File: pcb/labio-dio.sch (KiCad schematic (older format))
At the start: 0 parts

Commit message: add schematics for display and dio (dpad, servo, motor, encoder)
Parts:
- added C? (x5): C_Small, symbol C_Small
- added C? (x2): 0.1uF, symbol C_Small
- added P? (x5): CONN_01X03, symbol CONN_01X03
- added P? (x2): CONN_01X05, symbol CONN_01X05
- added P? (x3): CONN_01X02, symbol CONN_01X02
- added SW? (x5): SW_PUSH, symbol SW_PUSH
- added U?: L298P, symbol L298P
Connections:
- new net: P?.2 (P2), P?.4 (P4), P?.4 (P4)
- new net DPAD_CENTER: C?.1, SW?.1
- new net DPAD_DOWN: C?.1, SW?.1
- new net DPAD_LEFT: C?.1, SW?.1
- new net DPAD_RIGHT: C?.1, SW?.1
- new net DPAD_UP: C?.1, SW?.1
- new net ENC0_A: P?.3 (P3)
- new net ENC0_B: P?.5 (P5)
- new net ENC0_IDX: P?.2 (P2)
- new net ENC1_A: P?.3 (P3)
- new net ENC1_B: P?.5 (P5)
- new net ENC1_IDX: P?.2 (P2)
- new net GND: C?.2, C?.2, C?.2, C?.2, C?.2, C?.2, C?.2, P?.1 (P1), P?.1 (P1), P?.1 (P1), P?.1 (P1), P?.1 (P1), P?.2 (P2), SW?.2, SW?.2, SW?.2, U?.1 (GND), U?.10 (GND), U?.11 (GND), U?.20 (GND)
- new net MOTOR_IN1: U?.7 (IN1)
- new net MOTOR_IN2: U?.9 (IN2)
- new net MOTOR_IN3: U?.13 (IN3)
- new net MOTOR_IN4: U?.15 (IN4)
- new net MOTOR_OUT1: P?.1 (P1), U?.4 (OUT1)
- new net MOTOR_OUT2: P?.2 (P2), U?.5 (OUT2)
- new net MOTOR_OUT3: P?.1 (P1), U?.16 (OUT3)
- new net MOTOR_OUT4: P?.2 (P2), U?.17 (OUT4)
- new net MOTOR_SENSEA: P?.3 (P3), U?.2 (SENSEA)
- new net MOTOR_SENSEB: P?.2 (P2), U?.19 (SENSEB)
- new net PWM0: P?.3 (P3), U?.8 (ENABLEA)
- new net PWM1: P?.3 (P3), U?.14 (ENABLEB)
- new net VDD_3V3: C?.1, P?.1 (P1), U?.12 (VSS)
- new net VDD_5V: P?.3 (P3), P?.3 (P3)
- new net VMOTOR: C?.1, P?.1 (P1), P?.1 (P1), U?.6 (VS)
- new net VSERVO: P?.2 (P2), P?.2 (P2), P?.2 (P2)
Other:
- note added: "D-Pad\nUse RPi pull-ups with optional C for decoupling.\nIndividual IO lines for interrupts."
- note added: "Motor Driver"
- note added: "Quadrature Encoder\nUS Digital S1 Pinout.\nJumper for 3V3 or 5V power."
- note added: "Servos\nGround, voltage, signal headers.\nJumper for VMOTOR or 5V power."

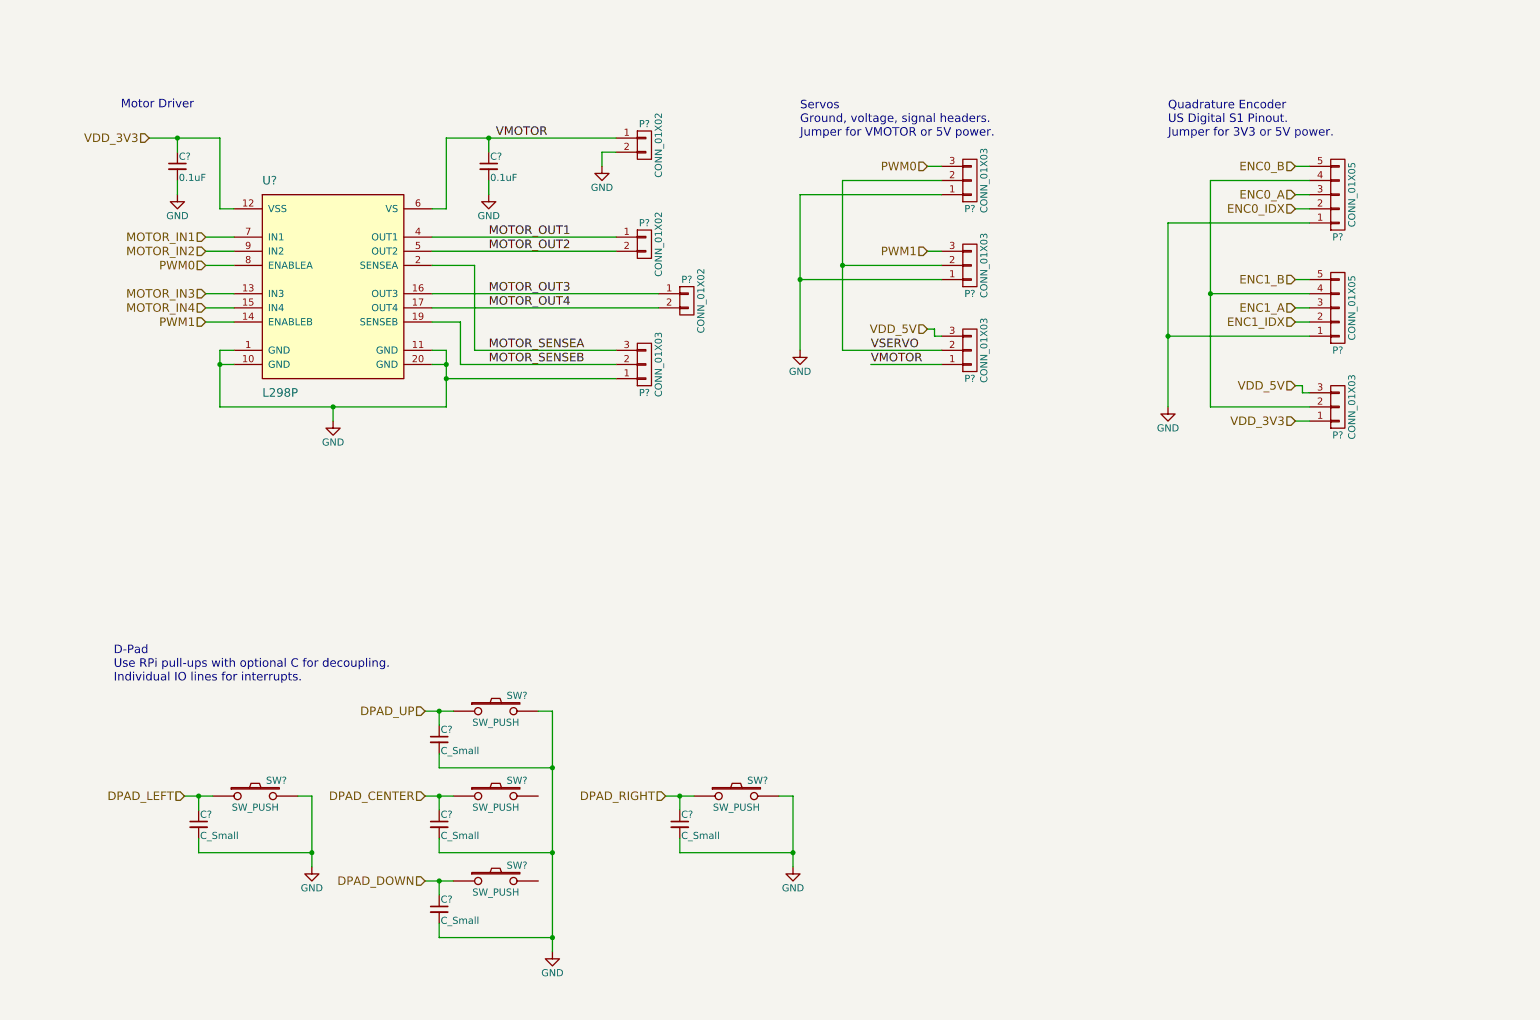
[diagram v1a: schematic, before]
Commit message: add imu sensors, make top level connections
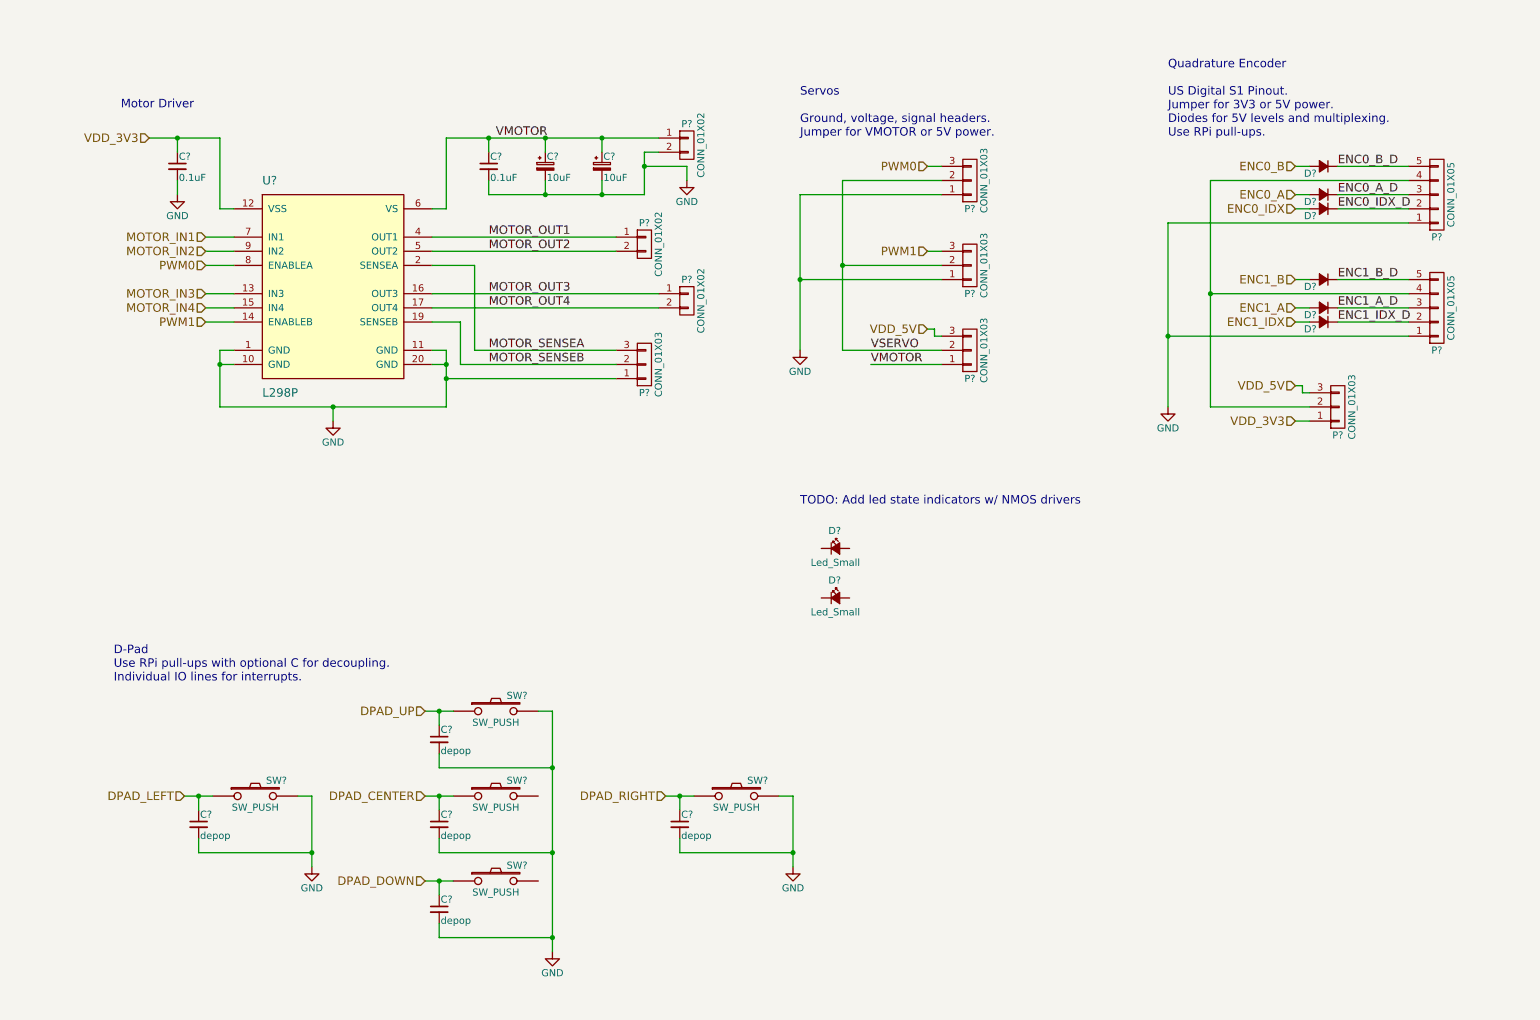
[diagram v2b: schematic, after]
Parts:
- added C? (x2): 10uF, symbol CP_Small
- added D? (x2): Led_Small, symbol Led_Small
- added D? (x6): D_Small, symbol D_Small
- C? (x5): value C_Small -> depop
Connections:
- net ENC0_A: now also D?.2 (A); no longer P?.3 (P3)
- net ENC0_B: now also D?.2 (A); no longer P?.5 (P5)
- net ENC0_IDX: now also D?.2 (A); no longer P?.2 (P2)
- net ENC1_A: now also D?.2 (A); no longer P?.3 (P3)
- net ENC1_B: now also D?.2 (A); no longer P?.5 (P5)
- net ENC1_IDX: now also D?.2 (A); no longer P?.2 (P2)
- net GND: now also C?.2, C?.2
- net VMOTOR: now also C?.1, C?.1
- new net ENC0_A_D: D?.1 (K), P?.3 (P3)
- new net ENC0_B_D: D?.1 (K), P?.5 (P5)
- new net ENC0_IDX_D: D?.1 (K), P?.2 (P2)
- new net ENC1_A_D: D?.1 (K), P?.3 (P3)
- new net ENC1_B_D: D?.1 (K), P?.5 (P5)
- new net ENC1_IDX_D: D?.1 (K), P?.2 (P2)
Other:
- note added: "Quadrature Encoder\n\nUS Digital S1 Pinout.\nJumper for 3V3 or 5V power.\nDiodes for 5V levels and multiplexing.\nUse RPi pull-ups."
- note added: "Servos\n\nGround, voltage, signal headers.\nJumper for VMOTOR or 5V power."
- note added: "TODO: Add led state indicators w/ NMOS drivers"
- note removed: "Quadrature Encoder\nUS Digital S1 Pinout.\nJumper for 3V3 or 5V power."
- note removed: "Servos\nGround, voltage, signal headers.\nJumper for VMOTOR or 5V power."
- moved on the sheet: P?

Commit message: finish rpi to module connections
* use dip switches to disable/configure blocks
* add light sensor
* fix motor controller sense resistors
* fix overused jtag probe pins
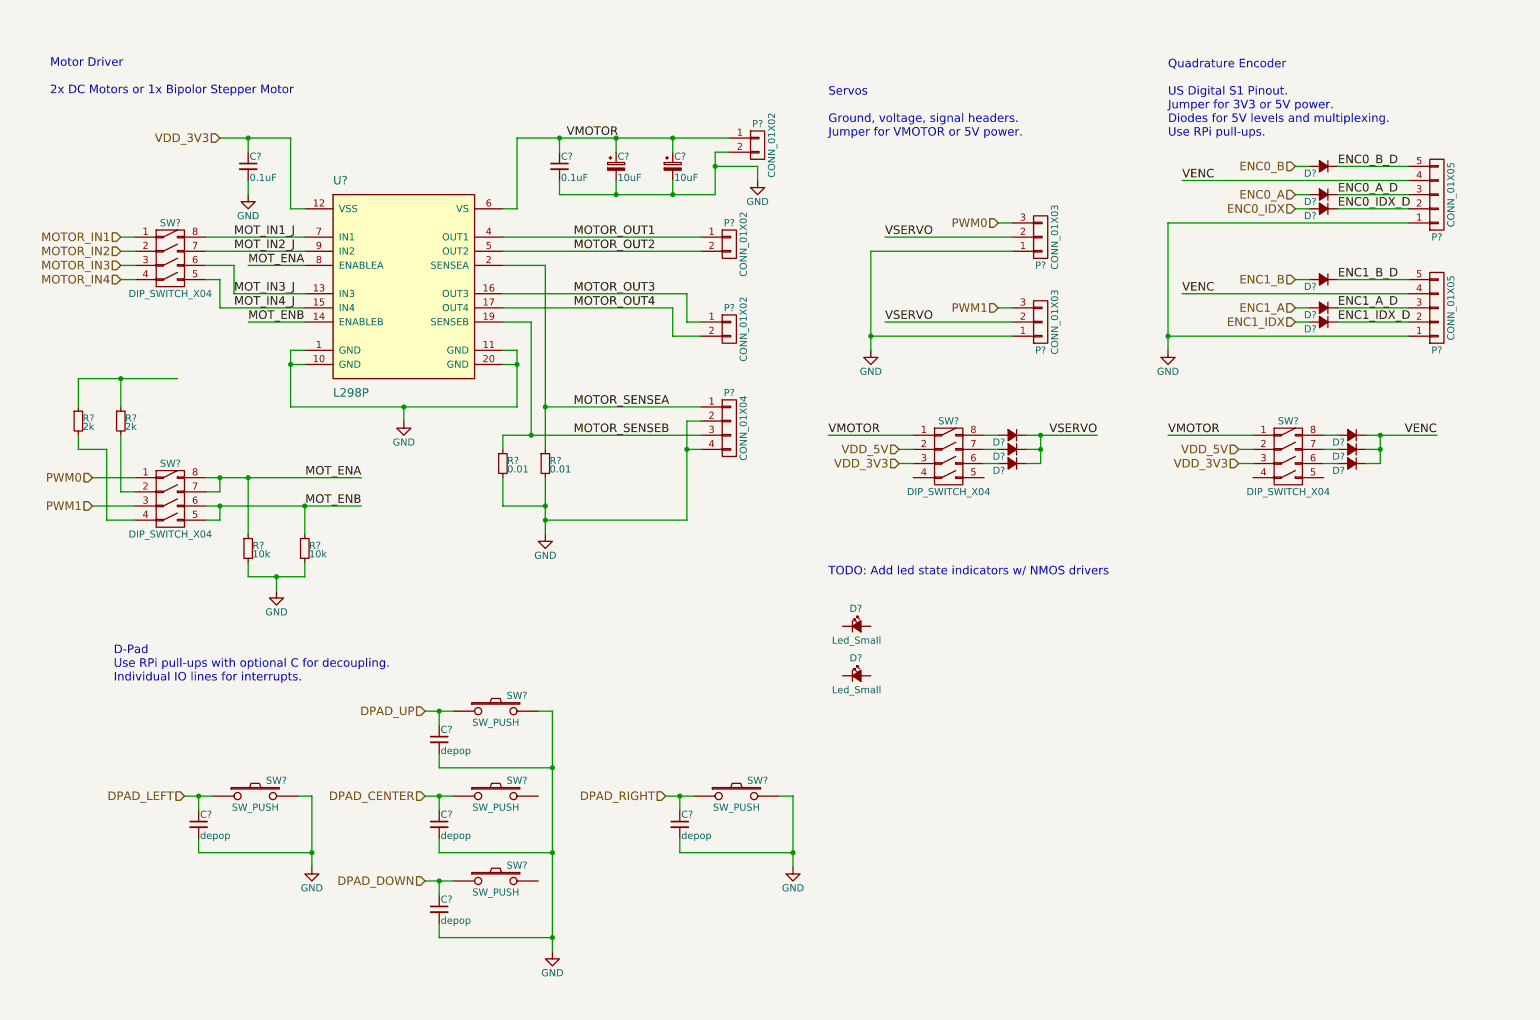
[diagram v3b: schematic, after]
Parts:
- removed P? (x3): CONN_01X03, symbol CONN_01X03
- added D? (x6): D_Small, symbol D_Small
- added P?: CONN_01X04, symbol CONN_01X04
- added R? (x2): 0.01, symbol R_Small
- added R? (x2): 10k, symbol R_Small
- added R? (x2): 2k, symbol R_Small
- added SW? (x4): DIP_SWITCH_X04, symbol DIP_SWITCH_X04
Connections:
- net GND: now also P?.2 (P2), P?.4 (P4), R?.2, R?.2, R?.2, R?.2
- net MOTOR_IN1: now also SW?.1 (1A); no longer U?.7 (IN1)
- net MOTOR_IN2: now also SW?.2 (2A); no longer U?.9 (IN2)
- net MOTOR_IN3: now also SW?.3 (3A); no longer U?.13 (IN3)
- net MOTOR_IN4: now also SW?.4 (4A); no longer U?.15 (IN4)
- net MOTOR_SENSEA: now also P?.1 (P1), R?.1
- net MOTOR_SENSEB: now also P?.3 (P3), R?.1
- net PWM0: now also SW?.1 (1A); no longer U?.8 (ENABLEA)
- net PWM1: now also SW?.3 (3A); no longer U?.14 (ENABLEB)
- net VDD_3V3: now also SW?.3 (3A), SW?.3 (3A)
- net VDD_5V: now also SW?.2 (2A), SW?.2 (2A)
- net VMOTOR: now also SW?.1 (1A), SW?.1 (1A)
- net VSERVO: now also D?.1 (K), D?.1 (K), D?.1 (K)
- net VENC: now reaches P?.4 (P4), P?.4 (P4)
- net VENC: now also D?.1 (K), D?.1 (K), D?.1 (K)
- new net: R?.2, SW?.2 (2A)
- new net: R?.2, SW?.4 (4A)
- new net: R?.1, R?.1
- new net: D?.2 (A), SW?.6 (3B) (x2)
- new net: D?.2 (A), SW?.7 (2A) (x2)
- new net: D?.2 (A), SW?.8 (1B) (x2)
- new net MOT_ENA: R?.1, SW?.7 (2A), SW?.8 (1B), U?.8 (ENABLEA)
- new net MOT_ENB: R?.1, SW?.5 (4B), SW?.6 (3B), U?.14 (ENABLEB)
- new net MOT_IN1_J: SW?.8 (1B), U?.7 (IN1)
- new net MOT_IN2_J: SW?.7 (2A), U?.9 (IN2)
- new net MOT_IN3_J: SW?.6 (3B), U?.13 (IN3)
- new net MOT_IN4_J: SW?.5 (4B), U?.15 (IN4)
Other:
- note added: "Motor Driver\n\n2x DC Motors or 1x Bipolor Stepper Motor"
- note removed: "Motor Driver"
- moved on the sheet: C?, D?, P?, U?

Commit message: add led status indicators, rotary encoder
* add led indicators for motor direction, pwm, encoder (muxed with dpad) pins
* add led indicators for power in all blocks
* split dpad into a different page
* add selectable onboard rotary encoder for testing or user input
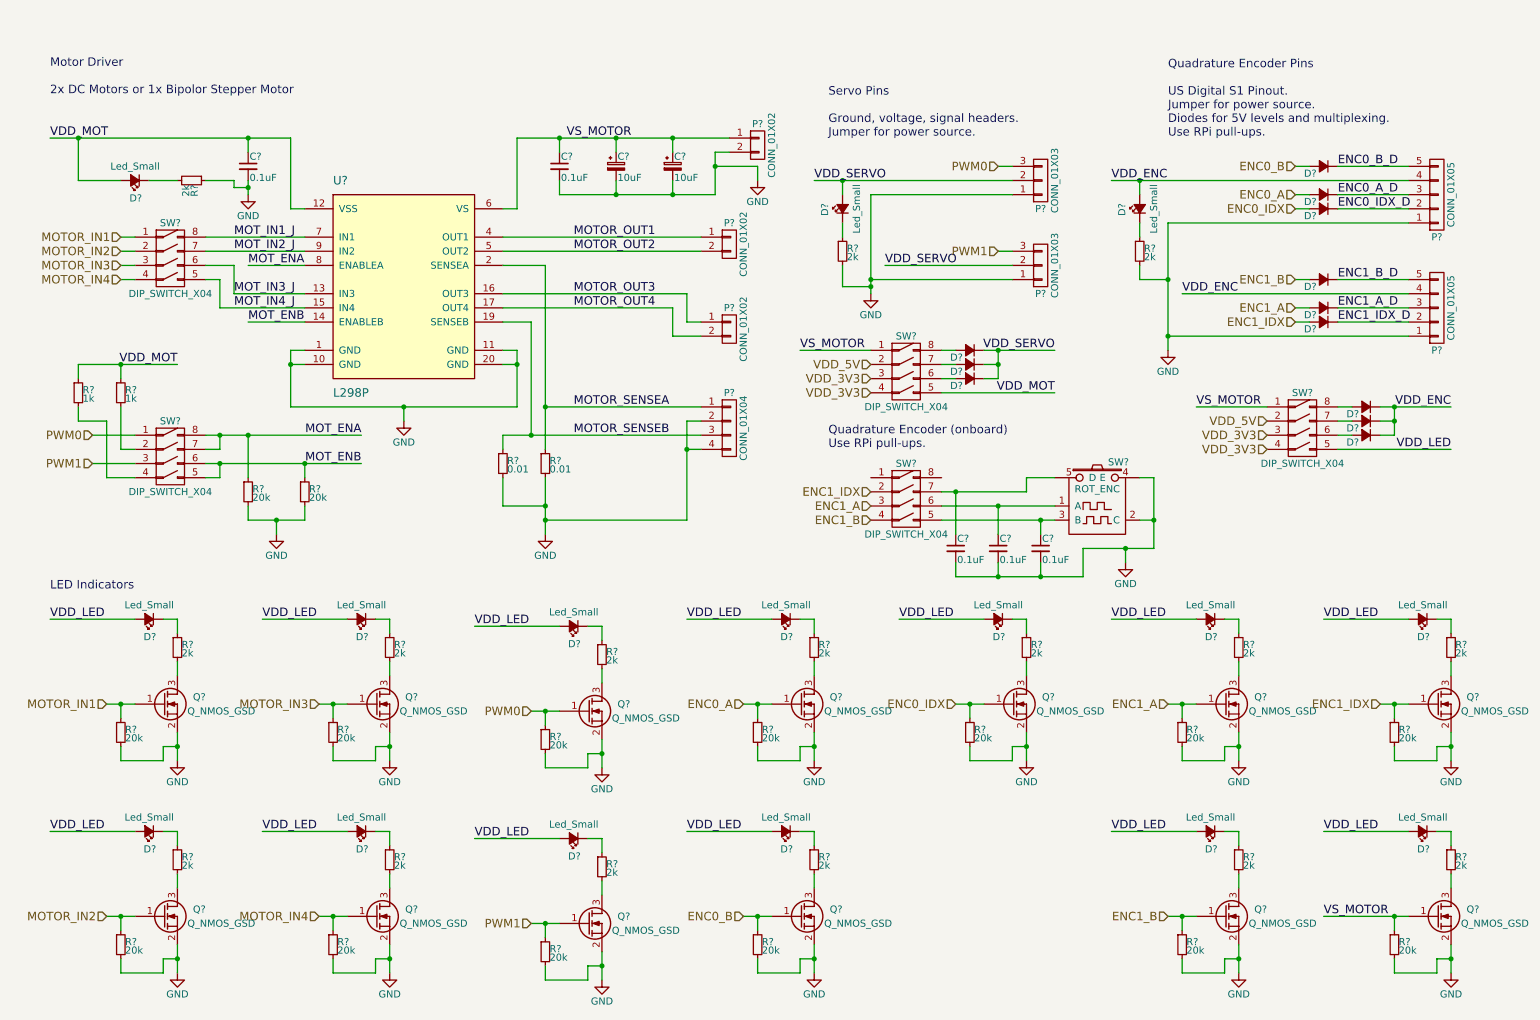
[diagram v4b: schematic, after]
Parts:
- removed C? (x5): depop, symbol C_Small
- removed D? (x2): Led_Small, symbol Led_Small
- removed SW? (x5): SW_PUSH, symbol SW_PUSH
- added C? (x3): 0.1uF, symbol C_Small
- added D? (x16): Led_Small, symbol Led_Small
- added Q? (x13): Q_NMOS_GSD, symbol Q_NMOS_GSD
- added R? (x16): 2k, symbol R_Small
- added R? (x13): 20k, symbol R_Small
- added SW?: DIP_SWITCH_X04, symbol DIP_SWITCH_X04
- added SW?: ROT_ENC, symbol ROT_ENC
- R? (x2): value 10k -> 20k
- R? (x2): value 2k -> 1k
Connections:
- net ENC0_A: now also Q?.1 (G), R?.1
- net ENC0_B: now also Q?.1 (G), R?.1
- net ENC0_IDX: now also Q?.1 (G), R?.1
- net ENC1_A: now also Q?.1 (G), R?.1, SW?.3 (3A)
- net ENC1_B: now also Q?.1 (G), R?.1, SW?.4 (4A)
- net ENC1_IDX: now also Q?.1 (G), R?.1, SW?.2 (2A)
- net GND: now also C?.2, C?.2, C?.2, Q?.2 (S), Q?.2 (S), Q?.2 (S), Q?.2 (S), Q?.2 (S), Q?.2 (S), Q?.2 (S), Q?.2 (S), Q?.2 (S), Q?.2 (S), Q?.2 (S), Q?.2 (S), Q?.2 (S), R?.1, R?.2, R?.2, R?.2, R?.2, R?.2, R?.2, R?.2, R?.2, R?.2, R?.2, R?.2, R?.2, R?.2, R?.2, R?.2, SW?.2 (C), SW?.4 (E)
- net MOTOR_IN1: now also Q?.1 (G), R?.1
- net MOTOR_IN2: now also Q?.1 (G), R?.1
- net MOTOR_IN3: now also Q?.1 (G), R?.1
- net MOTOR_IN4: now also Q?.1 (G), R?.1
- net PWM0: now also Q?.1 (G), R?.1
- net PWM1: now also Q?.1 (G), R?.1
- net VDD_3V3: now also SW?.4 (4A), SW?.4 (4A); no longer C?.1, U?.12 (VSS)
- net VDD_MOT: now reaches R?.1, R?.1
- net VDD_MOT: now also C?.1, SW?.5 (4B), U?.12 (VSS), D?.2 (A)
- net VDD_LED: now reaches SW?.5 (4B)
- net VDD_LED: now also D?.2 (A), D?.2 (A), D?.2 (A), D?.2 (A), D?.2 (A), D?.2 (A), D?.2 (A), D?.2 (A), D?.2 (A), D?.2 (A), D?.2 (A), D?.2 (A), D?.2 (A)
- net VENC renamed VDD_ENC
- net VDD_ENC: now also D?.2 (A)
- net VMOTOR renamed VS_MOTOR
- net VS_MOTOR: now also Q?.1 (G), R?.1
- net VSERVO renamed VDD_SERVO
- net VDD_SERVO: now also D?.2 (A)
- new net: D?.1 (K), R?.1 (x15)
- new net: Q?.3 (D), R?.2 (x13)
- new net: C?.1, SW?.3 (B), SW?.5 (4B)
- new net: C?.1, SW?.1 (A), SW?.6 (3B)
- new net: C?.1, SW?.5 (D), SW?.7 (2A)
- new net: D?.1 (K), R?.2
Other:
- note added: "LED Indicators"
- note added: "Quadrature Encoder (onboard)\nUse RPi pull-ups."
- note added: "Quadrature Encoder Pins\n\nUS Digital S1 Pinout.\nJumper for power source.\nDiodes for 5V levels and multiplexing.\nUse RPi pull-ups."
- note added: "Servo Pins\n\nGround, voltage, signal headers.\nJumper for power source."
- note removed: "D-Pad\nUse RPi pull-ups with optional C for decoupling.\nIndividual IO lines for interrupts."
- note removed: "Quadrature Encoder\n\nUS Digital S1 Pinout.\nJumper for 3V3 or 5V power.\nDiodes for 5V levels and multiplexing.\nUse RPi pull-ups."
- note removed: "Servos\n\nGround, voltage, signal headers.\nJumper for VMOTOR or 5V power."
- note removed: "TODO: Add led state indicators w/ NMOS drivers"
- moved on the sheet: D?, P?, R?, SW?
